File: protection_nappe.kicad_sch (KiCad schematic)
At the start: 33 parts

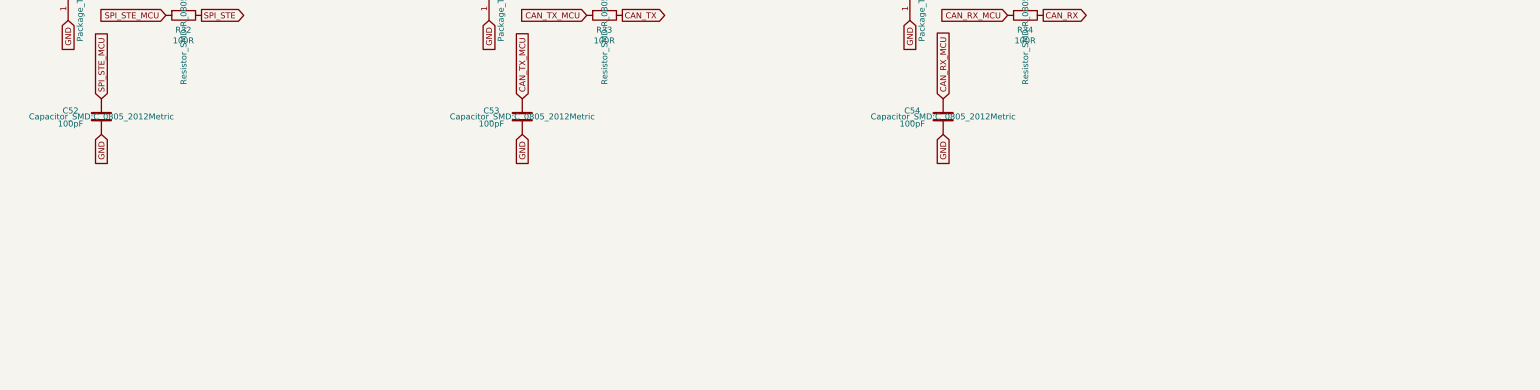
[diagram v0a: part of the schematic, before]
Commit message: CLB du F28P551 en mini-CPLD : report devkit, 4 trios, nappe logic (decision #20)
- Report sur connecteur_devkit.kicad_sch (symboles + labels reels, lib
  externe incluse) du reseequencement devkit (Iin/Iout/V1/Temp1/Temp2/
  ADC_8-12/I_SHUNT*_CMP/I_SHUNT*_MES deplaces) et des 4 broches neuves
  (Stage1_EN=GPIO9, Stage2_EN=GPIO20, HV_EN=GPIO21, Discharge=GPIO41).
- Corrige un erratum trouve en verifiant : protection_devkit3.kicad_sch
  gardait l'ancien nom nFAULT_MCU apres le renommage du connecteur en
  ~{FAULT_MCU}, coupant silencieusement le trio existant (meme categorie
  de bug que l'erratum ADC-2 de la decision #19).
- 4 nouveaux trios de protection D36-39/R35-38/C55-58, R=10R (signaux
  classes Rapide, decision explicite), pour les 4 sorties neuves.
- Nappe GPIO-2 renommee nappe "logic" (NAPPE_LOGIC, J13) : 9 reserves
  deviennent CLB_Out_1-4/CLB_In_1-5 (noms cosmetiques sur le connecteur
  uniquement, le net electrique reste le vrai nom de signal). 4 sorties
  protegees + 5 entrees tapees sans sacrifice (CAN_RX/CAN_TX, PWM2_B/
  PWM3_B/PWM4_B - deja protegees ailleurs, lues en plus ici).
- netclass_patterns, used_designators, doc/decisions.md #20,
  doc/nappes-shield.md, doc/brochage-devkit.csv mis a jour.

ERC : isolated_pin_label 9->5 (reste les 5 reserves ADC libres, hors
perimetre), pin_not_connected -9 (nappe logic cablee), aucune nouvelle
categorie.
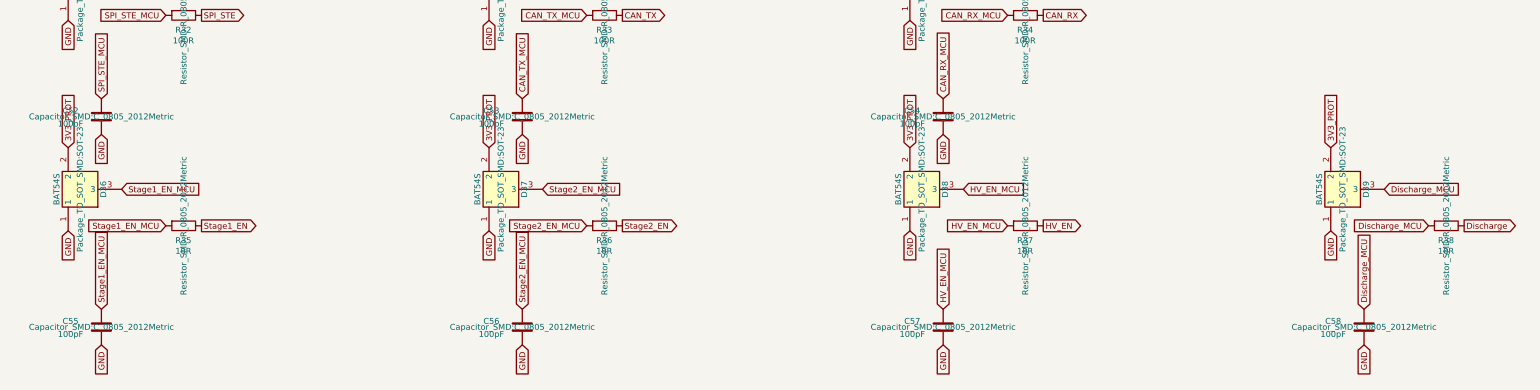
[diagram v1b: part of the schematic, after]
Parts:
- added C55, C56, C57, C58: 100pF, Capacitor_SMD:C_0805_2012Metric, symbol Device:C
- added D36, D37, D38, D39: BAT54S, Package_TO_SOT_SMD:SOT-23, symbol Power_Parts:BAT54S
- added R35, R36, R37, R38: 10R, Resistor_SMD:R_0805_2012Metric, symbol Device:R
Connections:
- net 3V3_PROT: now also D36.2, D37.2, D38.2, D39.2
- net GND: now also C55.1, C56.1, C57.1, C58.1, D36.1, D37.1, D38.1, D39.1
- new net Discharge: R38.1
- new net Discharge_MCU: C58.2, D39.3, R38.2
- new net HV_EN: R37.1
- new net HV_EN_MCU: C57.2, D38.3, R37.2
- new net Stage1_EN: R35.1
- new net Stage1_EN_MCU: C55.2, D36.3, R35.2
- new net Stage2_EN: R36.1
- new net Stage2_EN_MCU: C56.2, D37.3, R36.2
